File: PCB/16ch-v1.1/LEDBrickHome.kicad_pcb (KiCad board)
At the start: 2 copper layers, 67.6 x 44.5 mm, 61 parts, among them J1 USB4105-GF-A, J10 SM02B-SURS-TF, J11 SM02B-SURS-TF, J12 SM02B-SURS-TF, J13 SM02B-SURS-TF, J14 SM02B-SURS-TF, J15 SM02B-SURS-TF, J16 SM02B-SURS-TF, J17 SM02B-SURS-TF, J18 SM04B-SURS-TF, J19 SM04B-SURS-TF, J2 SM02B-SURS-TF, J20 SM04B-SURS-TF, J21 SM04B-SURS-TF, J22 SM04B-SURS-TF, J23 SM02B-SURS-TF, J3 SM02B-SURS-TF, J4 SM02B-SURS-TF, J5 SM02B-SURS-TF, J6 SM02B-SURS-TF, J7 SM02B-SURS-TF, J8 SM02B-SURS-TF, J9 SM02B-SURS-TF, Q1 BC817, Q10 2N7002K, Q11 2N7002K, Q12 2N7002K, Q13 2N7002K, Q14 2N7002K, Q15 2N7002K, Q16 2N7002K, Q17 2N7002K, Q18 2N7002K, Q2 BC817, Q3 2N7002K, Q4 2N7002K, Q5 2N7002K, Q6 2N7002K, Q7 2N7002K, Q8 2N7002K, Q9 2N7002K, SW1 KMR221G, SW2 KMR221G, U1 CH340C, U2 AZ1117IH-3.3TRG1, U4 ESP32-WROOM-32E-N16

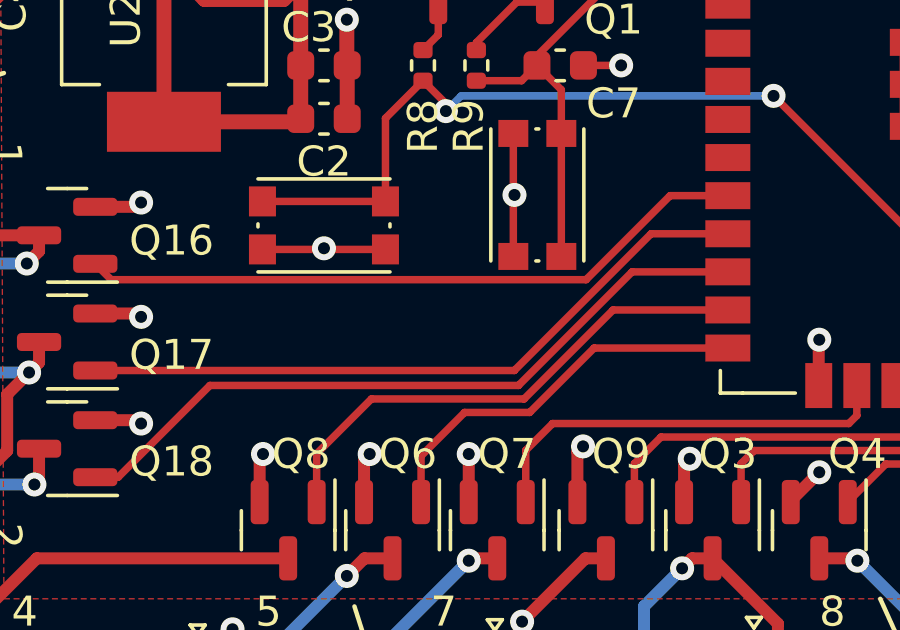
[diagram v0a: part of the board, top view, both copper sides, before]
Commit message: Add missing Silkscreen + fix spelling mistake
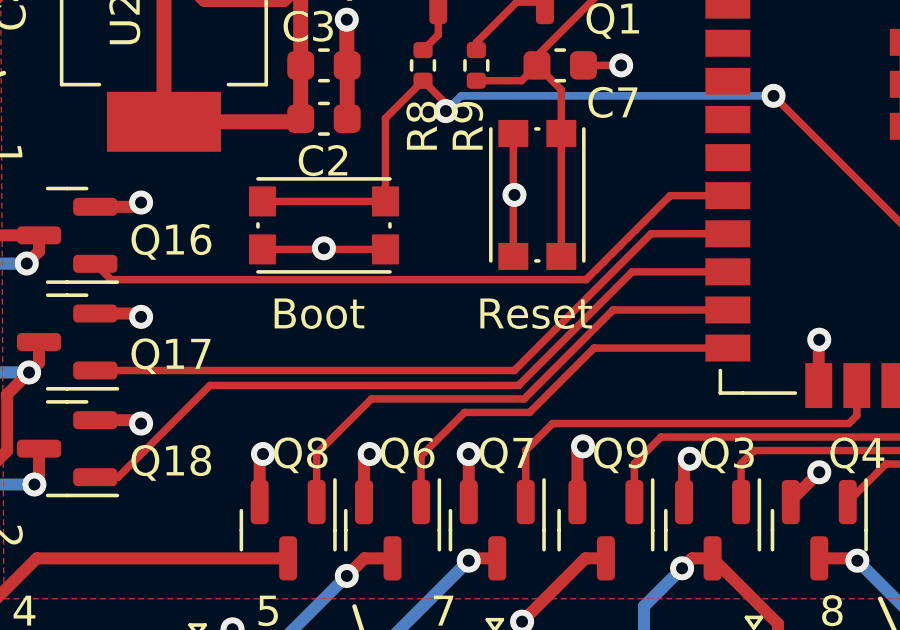
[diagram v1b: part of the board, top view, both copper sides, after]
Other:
- board text added: "Boot"
- board text added: "Reset"
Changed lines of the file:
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@@
+    (effects (font (size 1 1) (thickness 0.15)) (justify left bottom))
+  )
+  (gr_text "Reset" (at 49.784 74.676) (layer "F.SilkS")
     (effects (font (size 1 1) (thickness 0.15)) (justify left bottom))
   )
@@
     (effects (font (size 1 1) (thickness 0.15)) (justify left bottom))
   )
+  (gr_text "Boot" (at 42.926 74.676) (layer "F.SilkS")
+    (effects (font (size 1 1) (thickness 0.15)) (justify left bottom))
+  )

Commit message: Update URL
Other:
- board text added: "https://github.com/SenseAtHome/LEDBrickHome 16ch-v1.1"
- board text removed: "https://github.com/AlexCPU/LEDBrickHome 16ch-v1.1"
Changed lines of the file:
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@@
     (effects (font (size 1 1) (thickness 0.15)) (justify left bottom mirror))
   )
-  (gr_text "https://github.com/AlexCPU/LEDBrickHome\n16ch-v1.1" (at 74.676 75.438) (layer "B.SilkS")
+  (gr_text "https://github.com/SenseAtHome/LEDBrickHome\n16ch-v1.1" (at 74.676 75.438) (layer "B.SilkS")
     (effects (font (size 1 1) (thickness 0.15)) (justify left bottom mirror))
   )
